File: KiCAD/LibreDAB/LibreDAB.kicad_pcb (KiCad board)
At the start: 4 copper layers, 92 x 92 mm, 72 parts, among them J1 HX PM2.54-1X4P TP H8.5-ZQ, J2 TS30050050-040, J3 TS30050050-040, J4 HX PM2.54-1X4P TP H8.5-ZQ, J5 HX PM2.54-1X4P TP H8.5-ZQ, J6 HX PM2.54-1X4P TP H8.5-ZQ, J7 TS30050050-040, J8 TS30050050-040, Q1 SP010N01BGHTO, Q2 SP010N01BGHTO, Q3 SP010N01BGHTO, Q4 SP010N01BGHTO, U1 UCC27211DDAR, U2 10 MHz Opamp, U3 10 MHz Opamp, U4 10 MHz Opamp, U5 UCC27211DDAR

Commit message: PCB updates, getting ready for review
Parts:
- moved TP19 1.44 mm to (117.2, 117.3)
- moved TP15 1.32 mm to (91.4, 118.1)
- moved H2 0.85 mm to (129.8, 86.8)
- moved H4 0.79 mm to (129.8, 169.2)
- moved U4 0.43 mm to (74.4, 143.4)
- moved U3 0.41 mm to (61.3, 143.5)
- moved H1 0.35 mm to (47.2, 86.8)
- moved H3 0.35 mm to (47.2, 169.2)
- moved U2 0.34 mm to (53.2, 143.5)
- moved R14 0.31 mm to (110.6, 113.2)
- moved TP6 0.29 mm to (66.1, 97.8)
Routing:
- net /LV_Bridge/V_LV+: track 69.3 -> 1.44 mm, vias 32 -> 240
- net /LV_Bridge/LSW2: track 51.4 -> 20.6 mm, vias 2 -> 26
- net GND: track 142.5 -> 117.1 mm, vias 18 -> 79
- net /LV_Bridge/LSW1: track 52.2 -> 27.4 mm, vias 2 -> 23
- net +12V: track 79.8 -> 98.1 mm
- net /LV_Bridge/V_LV-: track 29.4 -> 17.7 mm, vias 0 -> 14
- net /LV_Bridge/I_LVsense: track 39.1 -> 40.3 mm
- net +5V: track 56.3 -> 57.1 mm
- net Net-(U3-IN+): track 6.55 -> 7.25 mm
- net /LV_Bridge/Vref: track 22.8 -> 23.3 mm
- added copper zone on B.Cu, net /LV_Bridge/LSW1
- added copper zone on In1.Cu, net /LV_Bridge/LSW1
- added copper zone on In2.Cu, net /LV_Bridge/LSW1
- added copper zone on B.Cu, net /LV_Bridge/LSW2
- added copper zone on In1.Cu, net /LV_Bridge/LSW2
- added copper zone on In2.Cu, net /LV_Bridge/LSW2
- added copper zone on B.Cu, net /LV_Bridge/V_LV-
- added copper zone on In1.Cu, net /LV_Bridge/V_LV-
- added copper zone on In2.Cu, net /LV_Bridge/V_LV-
- added copper zone on B.Cu, net GND

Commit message: Resolved various DRC issues. Almost ready for review
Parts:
- added D1: TVS DIODE 60VWM 96.8VC SMB(DO-214AA), lcsc_footprints:C49066953_SMB_L4_5-W3_7-LS5_4-RD, F.Cu at (54.3, 107.7)
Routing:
- net /LV_Bridge/V_LV-: vias 14 -> 18

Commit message: Minor edits getting ready for review
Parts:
- LOGO1: moved to F.Cu
- moved LOGO1 48.1 mm to (109.9, 165.9), turned to 0 degrees
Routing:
- net GND: vias 79 -> 78
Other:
- board text added: "LibreDAB LV Bridge rev 0.1 https://github.com/Stevie-Fairflow-Energy/LibreDAB 27/07/2026"

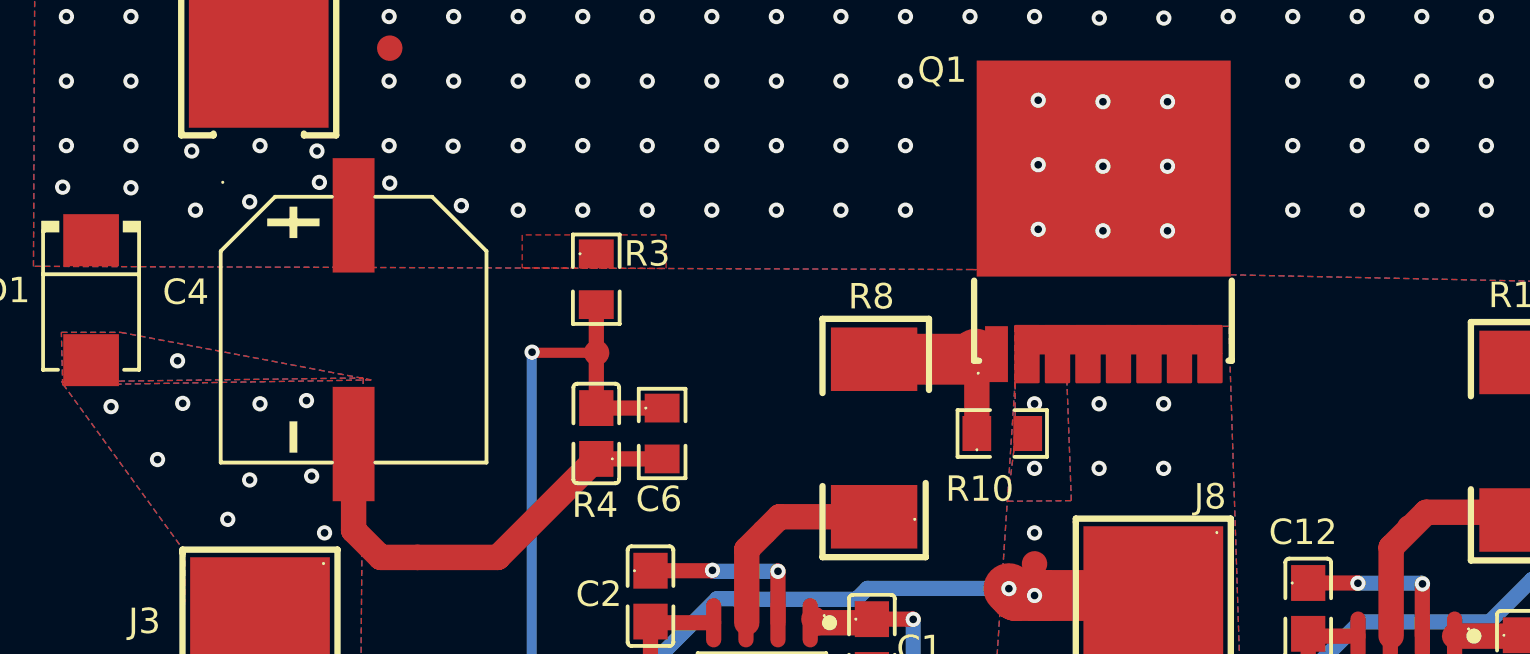
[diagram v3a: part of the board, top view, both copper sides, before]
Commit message: Added 100 V capacitors to PCB layout
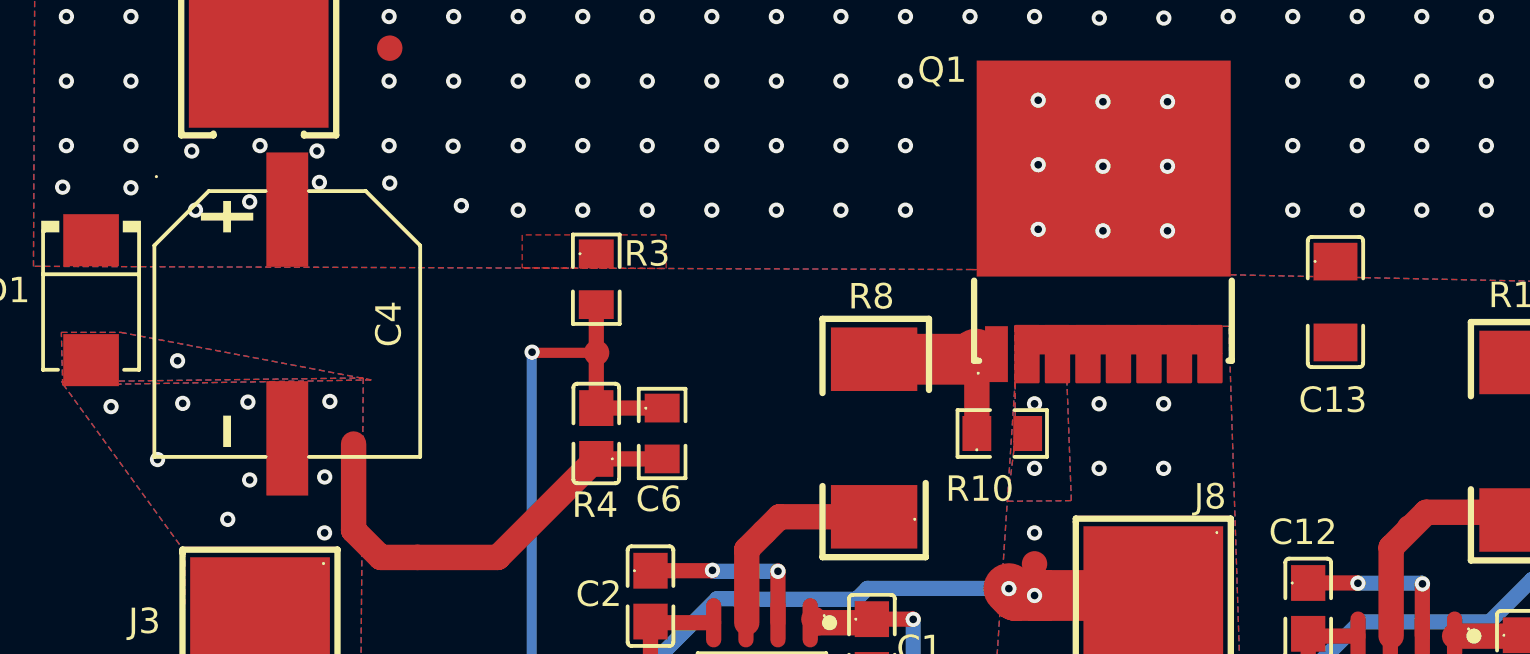
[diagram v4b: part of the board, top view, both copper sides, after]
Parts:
- added C13: 4.7uF ±10% 100V, lcsc_footprints:C41582415_C1206, F.Cu at (103.3, 107.8)
- C4: value 47uF, 80 V -> 47uF, 100 V
- moved C4 2.62 mm to (62.0, 108.6)

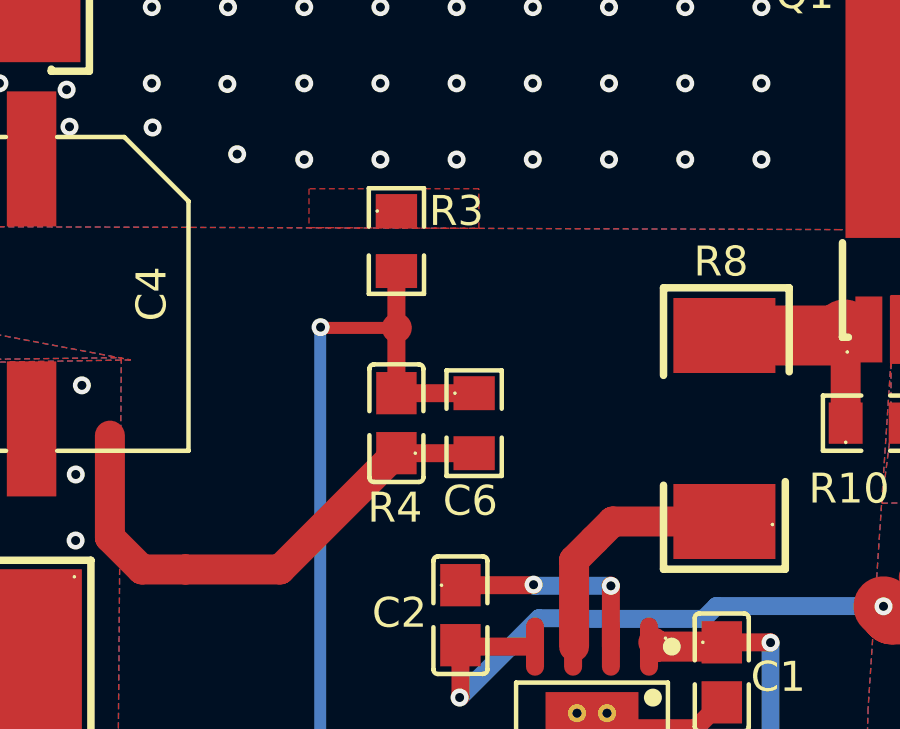
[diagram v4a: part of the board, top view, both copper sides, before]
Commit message: Updated Voltage divider to 1206 for top half and 0.1%
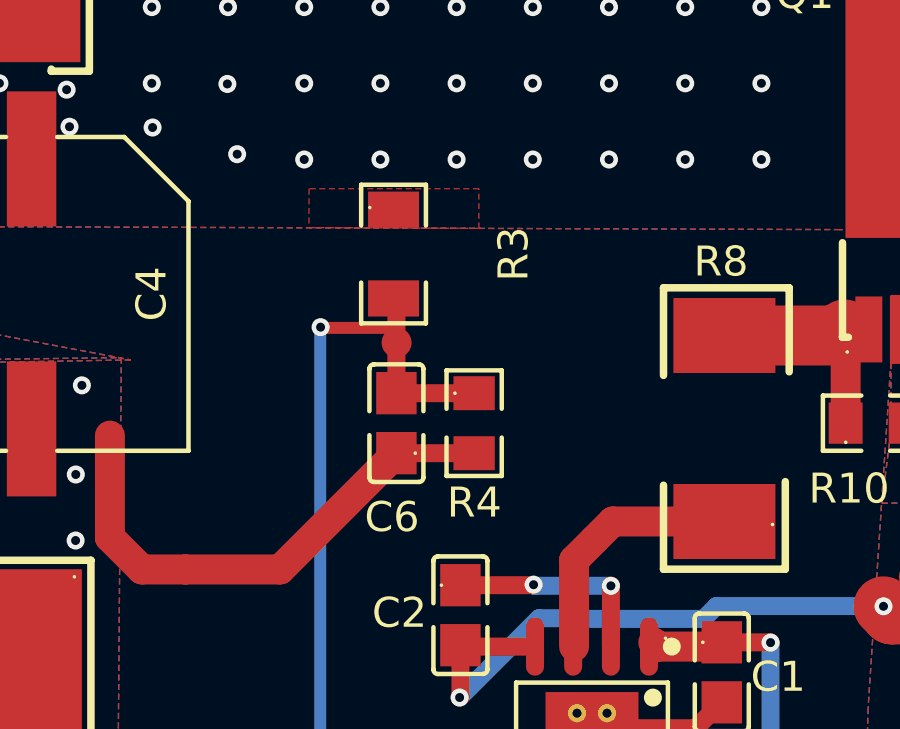
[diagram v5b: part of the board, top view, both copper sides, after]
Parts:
- R3: value 1MΩ (1004) ±1% -> 1MΩ ±0.1%; footprint lcsc_footprints:C17514_R0805 -> lcsc_footprints:C309662_R1206
- R4: value 25.5KΩ (2552) ±1% -> 25.5kΩ ±0.1%; footprint lcsc_footprints:C46670_R0805 -> lcsc_footprints:C865332_R0805
- moved TP8 0.49 mm to (74.2, 110.2)
- moved R3 0.44 mm to (74.1, 107.3)
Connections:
- R4 pad 1: /LV_Bridge/V_LV_Divider -> /LV_Bridge/V_LV-
- R4 pad 2: /LV_Bridge/V_LV- -> /LV_Bridge/V_LV_Divider
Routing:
- net /LV_Bridge/V_LV_Divider: track 50.4 -> 49.5 mm
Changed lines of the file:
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@@
 	(footprint "1Footprints:TestPoint_Pad_D1.0mm"
 		(layer "F.Cu")
-		(at 74.2061 109.7534)
+		(at 74.1992 110.2448)
 		(descr "SMD pad as test Point, diameter 1.0mm")
 		(tags "test point SMD pad")
@@
 		(descr "1nF (102) ±10% 50V")
 		(property "Reference" "C6"
-			(at -2.5908 2.4638 180)
+			(at -3.133 -0.1466 180)
 			(layer "F.SilkS")
 			(effects
@@
 		(embedded_fonts no)
 	)
-	(footprint "lcsc_footprints:C17514_R0805"
+	(footprint "lcsc_footprints:C309662_R1206"
 		(layer "F.Cu")
-		(at 74.1934 106.8578 -90)
-		(descr "1MΩ (1004) ±1%")
+		(at 74.0976 107.2916 -90)
 		(property "Reference" "R3"
-			(at -1 -2 180)
+			(at 0 -4 270)
 			(layer "F.SilkS")
 			(effects
@@
 			)
 		)
-		(property "Value" "1MΩ (1004) ±1%"
-			(at 0 4 90)
+		(property "Value" "1MΩ ±0.1%"
+			(at 0 4 270)
 			(layer "F.Fab")
 			(effects
@@
 			)
 		)
-		(property "Datasheet" "https://www.lcsc.com/datasheet/lcsc_datasheet_2206010200_UNI-ROYAL-Uniroyal-Elec-0805W8F1004T5E_C17514.pdf"
-			(at 0 0 90)
+		(property "Datasheet" "https://wmsc.lcsc.com/wmsc/upload/file/pdf/v2/lcsc/2304140030_YAGEO-RT1206BRD071ML_C309662.pdf"
+			(at 0 0 270)
 			(layer "F.Fab")
 			(hide yes)
@@
 			)
 		)
-		(property "Description" "1MΩ (1004) ±1%"
-			(at 0 0 90)
+		(property "Description" "RT1206BRD071ML"
+			(at 0 0 270)
 			(layer "F.Fab")
 			(hide yes)
@@
 			)
 		)
-		(property "LCSC Part" "C17514"
+		(property "LCSC Part" "C309662"
 			(at 0 0 270)
 			(layer "F.Fab")
@@
 			)
 		)
-		(property "LCSC" "C17514"
+		(property "LCSC" "C309662"
 			(at 0 0 270)
 			(unlocked yes)
@@
 			)
 		)
-		(property "Manufacturer" "UNI-ROYAL(厚声)"
+		(property "Manufacturer" "YAGEO(国巨)"
 			(at 0 0 270)
 			(unlocked yes)
@@
 		(attr smd)
 		(fp_line
-			(start -1.76 0.92)
-			(end -1.76 -0.92)
+			(start -2.31 1.08)
+			(end -2.31 -1.08)
 			(stroke
 				(width 0.15)
@@
 		)
 		(fp_line
-			(start -0.48 0.92)
-			(end -1.76 0.92)
+			(start -0.95 1.08)
+			(end -2.31 1.08)
 			(stroke
 				(width 0.15)
@@
 		)
 		(fp_line
-			(start 0.48 0.92)
-			(end 1.76 0.92)
+			(start 0.95 1.08)
+			(end 2.31 1.08)
 			(stroke
 				(width 0.15)
@@
 		)
 		(fp_line
-			(start 1.76 0.92)
-			(end 1.76 -0.92)
+			(start 2.31 1.08)
+			(end 2.31 -1.08)
 			(stroke
 				(width 0.15)
@@
 		)
 		(fp_line
-			(start -1.76 -0.92)
-			(end -0.48 -0.92)
+			(start -2.31 -1.08)
+			(end -0.95 -1.08)
 			(stroke
 				(width 0.15)
@@
 		)
 		(fp_line
-			(start 1.76 -0.92)
-			(end 0.48 -0.92)
+			(start 2.31 -1.08)
+			(end 0.95 -1.08)
 			(stroke
 				(width 0.15)
@@
 		)
 		(fp_circle
-			(center -1 0.64)
-			(end -0.97 0.64)
+			(center -1.55 0.79)
+			(end -1.52 0.79)
 			(stroke
 				(width 0.06)
@@
 		)
 		(fp_line
-			(start -1 0.64)
-			(end -1 -0.64)
+			(start -1.55 0.79)
+			(end -1.55 -0.79)
 			(stroke
 				(width 0.05)
@@
 		)
 		(fp_line
-			(start 1 0.64)
-			(end -1 0.64)
+			(start 1.55 0.79)
+			(end -1.55 0.79)
 			(stroke
 				(width 0.05)
@@
 		)
 		(fp_line
-			(start -1 -0.64)
-			(end 1 -0.64)
+			(start -1.55 -0.79)
+			(end 1.55 -0.79)
 			(stroke
 				(width 0.05)
@@
 		)
 		(fp_line
-			(start 1 -0.64)
-			(end 1 0.64)
+			(start 1.55 -0.79)
+			(end 1.55 0.79)
 			(stroke
 				(width 0.05)
@@
 		)
 		(fp_text user "${REFERENCE}"
-			(at 0 0 90)
+			(at 0 0 270)
 			(layer "F.Fab")
 			(effects
@@
 		)
 		(pad "1" smd rect
-			(at -1 0 270)
-			(size 1.133 1.377)
+			(at -1.48 0 270)
+			(size 1.208 1.701)
 			(layers "F.Cu" "F.Mask" "F.Paste")
 			(net 1 "/LV_Bridge/V_LV+")
 			(pinfunction "1")
-			(pintype "input")
+			(pintype "unspecified")
 		)
 		(pad "2" smd rect
-			(at 1 0 270)
-			(size 1.133 1.377)
+			(at 1.48 0 270)
+			(size 1.208 1.701)
 			(layers "F.Cu" "F.Mask" "F.Paste")
 			(net 3 "/LV_Bridge/V_LV_Divider")
 			(pinfunction "2")
-			(pintype "input")
+			(pintype "unspecified")
 		)
 		(embedded_fonts no)
-		(model "${KIPRJMOD}/libs/lcsc/3dmodels/C17514.wrl"
+		(model "${KIPRJMOD}/libs/lcsc/3dmodels/C309662.wrl"
 			(offset
-				(xyz 1.5 0 0)
+				(xyz 0 0 0)
 			)
 			(scale
@@
 			)
 			(rotate
-				(xyz -0 -0 -0)
+				(xyz 0 0 0)
 			)
 		)
 	)
-	(footprint "lcsc_footprints:C46670_R0805"
+	(footprint "lcsc_footprints:C865332_R0805"
 		(layer "F.Cu")
 		(at 76.7842 112.9284 -90)
-		(descr "25.5KΩ (2552) ±1%")
 		(property "Reference" "R4"
-			(at 2.8194 2.6416 180)
+			(at 2.6504 -0.0058 0)
 			(layer "F.SilkS")
 			(effects
@@
 			)
 		)
-		(property "Value" "25.5KΩ (2552) ±1%"
-			(at 0 4 90)
+		(property "Value" "25.5kΩ ±0.1%"
+			(at 0 4 270)
 			(layer "F.Fab")
 			(effects
@@
 			)
 		)
-		(property "Datasheet" "https://www.lcsc.com/datasheet/lcsc_datasheet_2206010000_UNI-ROYAL-Uniroyal-Elec-0805W8F2552T5E_C46670.pdf"
-			(at 0 0 90)
+		(property "Datasheet" "https://wmsc.lcsc.com/wmsc/upload/file/pdf/v2/lcsc/2210081801_YAGEO-RT0805BRD0725K5L_C865332.pdf"
+			(at 0 0 270)
 			(layer "F.Fab")
 			(hide yes)
@@
 			)
 		)
-		(property "Description" "25.5KΩ (2552) ±1%"
-			(at 0 0 90)
+		(property "Description" "RT0805BRD0725K5L"
+			(at 0 0 270)
 			(layer "F.Fab")
 			(hide yes)
@@
 			)
 		)
-		(property "LCSC Part" "C46670"
+		(property "LCSC Part" "C865332"
 			(at 0 0 270)
 			(layer "F.Fab")
@@
 			)
 		)
-		(property "LCSC" "C46670"
+		(property "LCSC" "C865332"
 			(at 0 0 270)
 			(unlocked yes)
@@
 			)
 		)
-		(property "Manufacturer" "UNI-ROYAL(厚声)"
+		(property "Manufacturer" "YAGEO(国巨)"
 			(at 0 0 270)
 			(unlocked yes)
@@
 		(sheetname "/LV_Bridge/")
 		(sheetfile "LV_Bridge.kicad_sch")
-		(attr smd)
+		(attr through_hole)
 		(fp_line
 			(start -1.76 0.92)
@@
 		)
 		(fp_text user "${REFERENCE}"
-			(at 0 0 90)
+			(at 0 0 270)
 			(layer "F.Fab")
 			(effects
@@
 			(size 1.133 1.377)
 			(layers "F.Cu" "F.Mask" "F.Paste")
-			(net 3 "/LV_Bridge/V_LV_Divider")
+			(net 2 "/LV_Bridge/V_LV-")
 			(pinfunction "1")
-			(pintype "input")
+			(pintype "unspecified")
 		)
 		(pad "2" smd rect
@@
 			(size 1.133 1.377)
 			(layers "F.Cu" "F.Mask" "F.Paste")
-			(net 2 "/LV_Bridge/V_LV-")
+			(net 3 "/LV_Bridge/V_LV_Divider")
 			(pinfunction "2")
-			(pintype "input")
+			(pintype "unspecified")
 		)
 		(embedded_fonts no)
-		(model "${KIPRJMOD}/libs/lcsc/3dmodels/C46670.wrl"
+		(model "${KIPRJMOD}/libs/lcsc/3dmodels/C865332.wrl"
 			(offset
-				(xyz 1.5 0 0)
+				(xyz 0 0 0)
 			)
 			(scale
@@
 			)
 			(rotate
-				(xyz -0 -0 -0)
+				(xyz 0 0 0)
 			)
 		)
@@
 	)
 	(segment
-		(start 71.6915 109.7534)
-		(end 71.6661 109.728)
-		(width 0.4)
+		(start 74.1934 108.8674)
+		(end 74.0976 108.7716)
+		(width 0.6)
 		(layer "F.Cu")
 		(net 3)
@@
 	(segment
 		(start 74.1934 111.9284)
-		(end 74.1934 107.8578)
+		(end 74.1934 108.8674)
 		(width 0.6)
 		(layer "F.Cu")
 		(net 3)
+	)
+	(segment
+		(start 71.6915 109.7534)
+		(end 71.6661 109.728)
+		(width 0.4)
+		(layer "F.Cu")
+		(net 3)

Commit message: Review comments addressed or parked
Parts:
- H1, H2, H3, H4: footprint 1Footprints:MountingHole_Pad_SMD_BD5.6-D4.1 -> MountingHole:MountingHole_4.3mm_M4_DIN965_Pad
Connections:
- R4 pad 1: /LV_Bridge/V_LV- -> /LV_Bridge/V_LV_Divider
- R4 pad 2: /LV_Bridge/V_LV_Divider -> /LV_Bridge/V_LV-
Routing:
- net Net-(Q3-G): track 7.93 -> 3.46 mm
- net Net-(Q2-G): track 8.15 -> 3.69 mm
- net Net-(Q4-G): track 8.01 -> 3.74 mm
- net Net-(Q1-G): track 7.40 -> 3.32 mm
- added copper zone on F.Cu, net Net-(Q1-G)
- added copper zone on F.Cu, net Net-(Q2-G)
- added copper zone on F.Cu, net Net-(Q3-G)
- added copper zone on F.Cu, net Net-(Q4-G)
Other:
- board text added: "LibreDAB LV Bridge rev 0.1 https://github.com/Stevie-Fairflow-Energy/LibreDAB 21/08/2026"
- board text removed: "LibreDAB LV Bridge rev 0.1 https://github.com/Stevie-Fairflow-Energy/LibreDAB 27/07/2026"
